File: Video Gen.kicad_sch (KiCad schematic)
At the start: 35 parts, among them J18 Aux Video, K14 VIDEO OUT, Q3 2N3904

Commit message: update traces
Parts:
- removed K14: VIDEO OUT, symbol Connector:Conn_Coaxial_Power
- added K14: RCA Connector, Apple-II:VIDEO, symbol Apple-II:Video
- A10: footprint Package_DIP:DIP-16_W7.62mm_Socket -> Package_DIP:DIP-16_W7.62mm
- A2, B10, B11, B12, B13, B2, C11, C13, C14: footprint Apple:DIP-14_W7.62mm -> Package_DIP:DIP-14_W7.62mm
- A3, A8, A9, B4, B9: footprint Apple:DIP-16_W7.62mm -> Package_DIP:DIP-16_W7.62mm
- A5: footprint Apple:DIP-24_W15.24mm -> Package_DIP:DIP-24_W15.24mm
- B3: footprint Apple:DIP-8_W7.62mm -> Package_DIP:DIP-8_W7.62mm
- Cap13, Cap14: footprint (none) -> Capacitor_THT:C_Disc_D5.0mm_W2.5mm_P5.00mm
- Cap15: renamed from C15; footprint (none) -> Capacitor_THT:C_Disc_D5.0mm_W2.5mm_P5.00mm
- Cap2: footprint (none) -> Capacitor_THT:C_Disc_D7.0mm_W2.5mm_P5.00mm
- L1: footprint (none) -> Inductor_THT:L_Axial_L7.0mm_D3.3mm_P12.70mm_Horizontal_Fastron_MICC
- R10, R12, R13, R5, R9: footprint (none) -> Resistor_THT:R_Axial_DIN0207_L6.3mm_D2.5mm_P10.16mm_Horizontal
- R11: footprint (none) -> Potentiometer_THT:Potentiometer_Bourns_3266Y_Vertical
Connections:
- net GND: now also K14.1
- net at R10.2: now also K14.2
- no-connect marks 6 -> 7
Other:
- moved on the sheet: R10

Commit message: more tracing
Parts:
- K14: DigiKey (none) -> PJRAN1X1U03X-ND
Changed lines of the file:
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@@
       (effects (font (size 1.27 1.27)) hide)
     )
-    (pin "8")
-    (pin "9")
     (pin "1")
     (pin "10")
@@
     (pin "6")
     (pin "7")
+    (pin "8")
+    (pin "9")
     (instances
       (project "AppleII"
@@
     (pin "1")
     (pin "2")
-    (pin "4")
-    (pin "7")
-    (pin "8")
-    (pin "3")
-    (pin "6")
+    (pin "3")
+    (pin "4")
+    (pin "6")
+    (pin "7")
+    (pin "8")
     (instances
       (project "AppleII"
@@
       (effects (font (size 1.27 1.27)) hide)
     )
+    (pin "1")
+    (pin "2")
+    (pin "3")
+    (pin "4")
+    (pin "5")
+    (pin "6")
     (pin "8")
     (pin "9")
+    (pin "10")
     (pin "11")
-    (pin "7")
-    (pin "6")
-    (pin "10")
+    (pin "12")
+    (pin "13")
     (pin "14")
-    (pin "13")
-    (pin "1")
-    (pin "4")
-    (pin "5")
-    (pin "2")
-    (pin "3")
-    (pin "12")
+    (pin "7")
     (instances
       (project "AppleII"
@@
       (effects (font (size 1.27 1.27)) hide)
     )
-    (property "Datasheet" "" (at 215.392 67.31 0)
-      (effects (font (size 1.27 1.27)) hide)
-    )
+    (property "Datasheet" "https://www.switchcraft.com/assets/1/24/pjran1x1u__x_series_cd.pdf?4664" (at 215.392 67.31 0)
+      (effects (font (size 1.27 1.27)) hide)
+    )
+    (property "DigiKey" "PJRAN1X1U03X-ND" (at 215.392 67.31 0)
+      (effects (font (size 1.27 1.27)) hide)
+    )

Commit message: more tracing
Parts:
- removed CT3: 5-50pf, symbol AppleII-rescue:CTRIM_Small-Device
- added CT3: 5-50pF, Apple-II:COLOUR_TRIM, symbol Device:C_Trim_Differential
- J18: footprint (none) -> Connector_PinHeader_2.54mm:PinHeader_1x04_P2.54mm_Vertical
- Q3: footprint digikey-footprints:TO-92-3 -> Package_TO_SOT_THT:TO-92
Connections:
- net GND: now also CT3.1
- net at Cap2.1, L1.1, R5.2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: now also CT3.2
- no-connect marks 7 -> 8
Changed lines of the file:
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@@
   (no_connect (at 425.45 309.88))
   (no_connect (at 425.45 304.8))
+  (no_connect (at 119.38 201.93))
   (no_connect (at 425.45 240.03))
   (no_connect (at 485.14 170.18))
@@
     (stroke (width 0) (type default))
   )
-  (wire (pts (xy 121.92 200.66) (xy 121.92 203.2))
+  (wire (pts (xy 124.46 201.93) (xy 124.46 203.2))
     (stroke (width 0) (type default))
   )
@@
     (stroke (width 0) (type default))
   )
+  (wire (pts (xy 124.46 203.2) (xy 121.92 203.2))
+    (stroke (width 0) (type default))
+  )
   (wire (pts (xy 196.85 71.12) (xy 205.74 71.12))
     (stroke (width 0) (type default))
@@
     (stroke (width 0) (type default))
   )
-  (wire (pts (xy 121.92 195.58) (xy 121.92 191.77))
+  (wire (pts (xy 121.92 194.31) (xy 121.92 191.77))
     (stroke (width 0) (type default))
   )
@@
     )
   )
-  (symbol (lib_id "AppleII-rescue:CTRIM_Small-Device") (at 121.92 198.12 0) (unit 1)
-    (in_bom yes) (on_board yes) (dnp no)
-    (property "Reference" "CT3" (at 117.602 196.596 0)
-      (effects (font (size 1.27 1.27)) (justify left))
-    )
-    (property "Value" "5-50pf" (at 124.46 202.438 90)
-      (effects (font (size 1.27 1.27)) (justify left))
-    )
-    (property "Footprint" "" (at 121.92 198.12 0)
-      (effects (font (size 1.27 1.27)) hide)
-    )
-    (property "Datasheet" "~" (at 121.92 198.12 0)
-      (effects (font (size 1.27 1.27)) hide)
-    )
-    (pin "1")
-    (pin "2")
-    (instances
-      (project "AppleII"
-        (path "/f1f08369-4db3-46f7-9b89-a5d3cfbed55a/00000000-0000-0000-0000-0000632bf564"
-          (reference "CT3") (unit 1)
-        )
-      )
-    )
-  )
   (symbol (lib_id "power:GND") (at 121.92 204.47 0) (unit 1)
     (in_bom yes) (on_board yes) (dnp no)
@@
       (effects (font (size 1.27 1.27)) (justify right))
     )
-    (property "Footprint" "" (at 172.72 59.69 0)
+    (property "Footprint" "Connector_PinHeader_2.54mm:PinHeader_1x04_P2.54mm_Vertical" (at 172.72 59.69 0)
       (effects (font (size 1.27 1.27)) hide)
     )
@@
       (effects (font (size 1.524 1.524)) (justify left))
     )
-    (property "Footprint" "digikey-footprints:TO-92-3" (at 168.91 92.71 0)
+    (property "Footprint" "Package_TO_SOT_THT:TO-92" (at 168.91 92.71 0)
       (effects (font (size 1.524 1.524)) (justify left) hide)
     )
@@
         )
       )
+    )
+  )
+  (symbol (lib_id "Device:C_Trim_Differential") (at 121.92 198.12 180) (unit 1)
+    (in_bom yes) (on_board yes) (dnp no) (fields_autoplaced)
+    (property "Reference" "CT3" (at 127 196.977 0)
+      (effects (font (size 1.27 1.27)) (justify right))
+    )
+    (property "Value" "5-50pF" (at 127 199.517 0)
+      (effects (font (size 1.27 1.27)) (justify right))
+    )
+    (property "Footprint" "Apple-II:COLOUR_TRIM" (at 121.92 198.12 0)
+      (effects (font (size 1.27 1.27)) hide)
+    )
+    (property "Datasheet" "https://www.vishay.com/docs/28528/bfc2808-10mm.pdf" (at 121.92 198.12 0)
+      (effects (font (size 1.27 1.27)) hide)
+    )
+    (property "DigiKey" "BFC280831659-ND" (at 121.92 198.12 0)
+      (effects (font (size 1.27 1.27)) hide)
+    )
+    (pin "1")
+    (pin "2")
+    (pin "3")
+    (instances
+      (project "AppleII"
+        (path "/f1f08369-4db3-46f7-9b89-a5d3cfbed55a/00000000-0000-0000-0000-0000632bf564"
+          (reference "CT3") (unit 1)
+        )
+      )

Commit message: more tracing
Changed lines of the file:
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@@
-    (stroke (width 0) (type default))
-  )
-  (bus_entry (at 302.26 135.89) (size 2.54 2.54)
     (stroke (width 0) (type default))
   )
@@
     (stroke (width 0) (type default))
   )
-  (bus_entry (at 302.26 138.43) (size 2.54 2.54)
-    (stroke (width 0) (type default))
-  )
   (bus_entry (at 395.224 242.57) (size 2.54 2.54)
     (stroke (width 0) (type default))
   )
-  (bus_entry (at 302.26 133.35) (size 2.54 2.54)
-    (stroke (width 0) (type default))
-  )
   (bus_entry (at 395.224 234.95) (size 2.54 2.54)
     (stroke (width 0) (type default))
@@
     (stroke (width 0) (type default))
   )
-  (bus (pts (xy 294.64 130.81) (xy 302.26 130.81))
-    (stroke (width 0) (type default))
-  )
   (wire (pts (xy 36.83 374.65) (xy 34.29 374.65))
     (stroke (width 0) (type default))
@@
     (stroke (width 0) (type default))
   )
-  (bus (pts (xy 302.26 133.35) (xy 302.26 130.81))
-    (stroke (width 0) (type default))
-  )
   (wire (pts (xy 153.67 95.25) (xy 157.48 95.25))
     (stroke (width 0) (type default))
@@
     (stroke (width 0) (type default))
   )
-  (bus (pts (xy 302.26 138.43) (xy 302.26 135.89))
-    (stroke (width 0) (type default))
-  )
   (wire (pts (xy 149.86 63.5) (xy 149.86 64.77))
     (stroke (width 0) (type default))
@@
   )
   (wire (pts (xy 304.8 146.05) (xy 311.15 146.05))
-    (stroke (width 0) (type default))
-  )
-  (bus (pts (xy 302.26 135.89) (xy 302.26 133.35))
     (stroke (width 0) (type default))
   )
@@
     )
   )
+  (global_label "VB" (shape input) (at 304.8227 138.43 180) (fields_autoplaced)
+    (effects (font (size 1.27 1.27)) (justify right))
+    (property "Intersheetrefs" "${INTERSHEET_REFS}" (at 300.1331 138.43 0)
+      (effects (font (size 1.27 1.27)) (justify right) hide)
+    )
+  )
   (global_label "HIRES" (shape output) (at 151.13 325.12 0)
     (effects (font (size 1.27 1.27)) (justify left))
@@
     )
   )
+  (global_label "VA" (shape input) (at 304.8227 135.89 180) (fields_autoplaced)
+    (effects (font (size 1.27 1.27)) (justify right))
+    (property "Intersheetrefs" "${INTERSHEET_REFS}" (at 300.3145 135.89 0)
+      (effects (font (size 1.27 1.27)) (justify right) hide)
+    )
+  )
   (global_label "V2" (shape input) (at 43.942 322.58 180)
     (effects (font (size 1.27 1.27)) (justify right))
@@
     )
   )
-  (global_label "V[A..C]" (shape input) (at 294.64 130.81 180)
-    (effects (font (size 1.27 1.27)) (justify right))
-    (property "Intersheetrefs" "${INTERSHEET_REFS}" (at 294.64 130.81 0)
-      (effects (font (size 1.27 1.27)) hide)
-    )
-  )
   (global_label "LD[0..7]" (shape input) (at 395.224 232.918 0)
     (effects (font (size 1.27 1.27)) (justify left))
@@
     )
   )
+  (global_label "VC" (shape input) (at 304.8227 140.97 180) (fields_autoplaced)
+    (effects (font (size 1.27 1.27)) (justify right))
+    (property "Intersheetrefs" "${INTERSHEET_REFS}" (at 300.1331 140.97 0)
+      (effects (font (size 1.27 1.27)) (justify right) hide)
+    )
+  )

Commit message: finish tracing
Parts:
- added unit 7 of C11
- added unit 3 of C13
- added Cap16: 0.1uF, Capacitor_THT:C_Disc_D5.0mm_W2.5mm_P5.00mm, symbol Device:C_Small
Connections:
- net A8-6 is gone; now on net GND: A8.6 (I1b)
- net +5V: now also C11.14 (VCC), C13.14 (VCC), Cap16.2
- net GND: now also C11.7 (GND), C13.7 (GND), Cap16.1
- net A9-9 renamed B11-5

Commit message: beautify capacitor footprint
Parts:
- renumbered Cap16 to Cap47
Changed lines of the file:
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@@
   (symbol (lib_id "Device:C_Small") (at 499.11 182.88 270) (unit 1)
     (in_bom yes) (on_board yes) (dnp no)
-    (property "Reference" "Cap16" (at 500.888 183.134 0)
+    (property "Reference" "Cap47" (at 500.888 183.134 0)
       (effects (font (size 1.27 1.27)) (justify left))
     )
@@
     (instances
       (project "AppleII"
-        (path "/f1f08369-4db3-46f7-9b89-a5d3cfbed55a/00000000-0000-0000-0000-00006017a131"
-          (reference "Cap16") (unit 1)
-        )
         (path "/f1f08369-4db3-46f7-9b89-a5d3cfbed55a/00000000-0000-0000-0000-0000632bf564"
           (reference "Cap47") (unit 1)
@@
   (symbol (lib_id "power:GND") (at 501.65 182.88 90) (unit 1)
     (in_bom yes) (on_board yes) (dnp no)
-    (property "Reference" "#PWR015" (at 508 182.88 0)
+    (property "Reference" "#PWR03" (at 508 182.88 0)
       (effects (font (size 1.27 1.27)) hide)
     )
@@
     (instances
       (project "AppleII"
-        (path "/f1f08369-4db3-46f7-9b89-a5d3cfbed55a/00000000-0000-0000-0000-00006017a131"
-          (reference "#PWR015") (unit 1)
-        )
         (path "/f1f08369-4db3-46f7-9b89-a5d3cfbed55a/00000000-0000-0000-0000-0000632bf564"
           (reference "#PWR03") (unit 1)

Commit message: beautify resistors
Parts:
- Cap13, Cap14, Cap15, Cap47: footprint Capacitor_THT:C_Disc_D5.0mm_W2.5mm_P5.00mm -> Apple-II:C_Disc_D5.0mm_W2.5mm_P5.00mm
- R10, R12, R13, R5, R6, R7, R8, R9: footprint Resistor_THT:R_Axial_DIN0207_L6.3mm_D2.5mm_P10.16mm_Horizontal -> Apple-II:R_Axial_DIN0207_L6.3mm_D2.5mm_P10.16mm_Horizontal
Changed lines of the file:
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@@
       (effects (font (size 1.27 1.27)))
     )
-    (property "Footprint" "Resistor_THT:R_Axial_DIN0207_L6.3mm_D2.5mm_P10.16mm_Horizontal" (at 96.52 193.548 90)
+    (property "Footprint" "Apple-II:R_Axial_DIN0207_L6.3mm_D2.5mm_P10.16mm_Horizontal" (at 96.52 193.548 90)
       (effects (font (size 1.27 1.27)) hide)
     )
@@
       (effects (font (size 1.27 1.27)))
     )
-    (property "Footprint" "Resistor_THT:R_Axial_DIN0207_L6.3mm_D2.5mm_P10.16mm_Horizontal" (at 199.136 65.278 90)
+    (property "Footprint" "Apple-II:R_Axial_DIN0207_L6.3mm_D2.5mm_P10.16mm_Horizontal" (at 199.136 65.278 90)
       (effects (font (size 1.27 1.27)) hide)
     )
@@
       (effects (font (size 1.27 1.27)) (justify left))
     )
-    (property "Footprint" "Capacitor_THT:C_Disc_D5.0mm_W2.5mm_P5.00mm" (at 160.02 62.23 0)
+    (property "Footprint" "Apple-II:C_Disc_D5.0mm_W2.5mm_P5.00mm" (at 160.02 62.23 0)
       (effects (font (size 1.27 1.27)) hide)
     )
@@
       (effects (font (size 1.27 1.27)) (justify left))
     )
-    (property "Footprint" "Capacitor_THT:C_Disc_D5.0mm_W2.5mm_P5.00mm" (at 149.86 60.96 0)
+    (property "Footprint" "Apple-II:C_Disc_D5.0mm_W2.5mm_P5.00mm" (at 149.86 60.96 0)
       (effects (font (size 1.27 1.27)) hide)
     )
@@
       (effects (font (size 1.27 1.27)))
     )
-    (property "Footprint" "Resistor_THT:R_Axial_DIN0207_L6.3mm_D2.5mm_P10.16mm_Horizontal" (at 317.246 68.072 90)
+    (property "Footprint" "Apple-II:R_Axial_DIN0207_L6.3mm_D2.5mm_P10.16mm_Horizontal" (at 317.246 68.072 90)
       (effects (font (size 1.27 1.27)) hide)
     )
@@
       (effects (font (size 1.27 1.27)) (justify left))
     )
-    (property "Footprint" "Capacitor_THT:C_Disc_D5.0mm_W2.5mm_P5.00mm" (at 315.468 76.962 0)
+    (property "Footprint" "Apple-II:C_Disc_D5.0mm_W2.5mm_P5.00mm" (at 315.468 76.962 0)
       (effects (font (size 1.27 1.27)) hide)
     )
@@
       (effects (font (size 1.27 1.27)))
     )
-    (property "Footprint" "Resistor_THT:R_Axial_DIN0207_L6.3mm_D2.5mm_P10.16mm_Horizontal" (at 317.246 60.452 90)
+    (property "Footprint" "Apple-II:R_Axial_DIN0207_L6.3mm_D2.5mm_P10.16mm_Horizontal" (at 317.246 60.452 90)
       (effects (font (size 1.27 1.27)) hide)
     )
@@
       (effects (font (size 1.27 1.27)))
     )
-    (property "Footprint" "Resistor_THT:R_Axial_DIN0207_L6.3mm_D2.5mm_P10.16mm_Horizontal" (at 165.1 127.762 90)
+    (property "Footprint" "Apple-II:R_Axial_DIN0207_L6.3mm_D2.5mm_P10.16mm_Horizontal" (at 165.1 127.762 90)
       (effects (font (size 1.27 1.27)) hide)
     )
@@
       (effects (font (size 1.27 1.27)))
     )
-    (property "Footprint" "Resistor_THT:R_Axial_DIN0207_L6.3mm_D2.5mm_P10.16mm_Horizontal" (at 175.768 143.51 90)
+    (property "Footprint" "Apple-II:R_Axial_DIN0207_L6.3mm_D2.5mm_P10.16mm_Horizontal" (at 175.768 143.51 90)
       (effects (font (size 1.27 1.27)) hide)
     )
@@
       (effects (font (size 1.27 1.27)))
     )
-    (property "Footprint" "Resistor_THT:R_Axial_DIN0207_L6.3mm_D2.5mm_P10.16mm_Horizontal" (at 184.15 131.318 90)
+    (property "Footprint" "Apple-II:R_Axial_DIN0207_L6.3mm_D2.5mm_P10.16mm_Horizontal" (at 184.15 131.318 90)
       (effects (font (size 1.27 1.27)) hide)
     )
@@
       (effects (font (size 1.27 1.27)))
     )
-    (property "Footprint" "Resistor_THT:R_Axial_DIN0207_L6.3mm_D2.5mm_P10.16mm_Horizontal" (at 161.29 97.028 90)
+    (property "Footprint" "Apple-II:R_Axial_DIN0207_L6.3mm_D2.5mm_P10.16mm_Horizontal" (at 161.29 97.028 90)
       (effects (font (size 1.27 1.27)) hide)
     )
@@
       (effects (font (size 1.27 1.27)) (justify left))
     )
-    (property "Footprint" "Capacitor_THT:C_Disc_D5.0mm_W2.5mm_P5.00mm" (at 499.11 182.88 0)
-      (effects (font (size 1.27 1.27)) hide)
-    )
+    (property "Footprint" "Apple-II:C_Disc_D5.0mm_W2.5mm_P5.00mm" (at 499.11 182.88 0)
+      (effects (font (size 1.27 1.27)) hide)
+    )

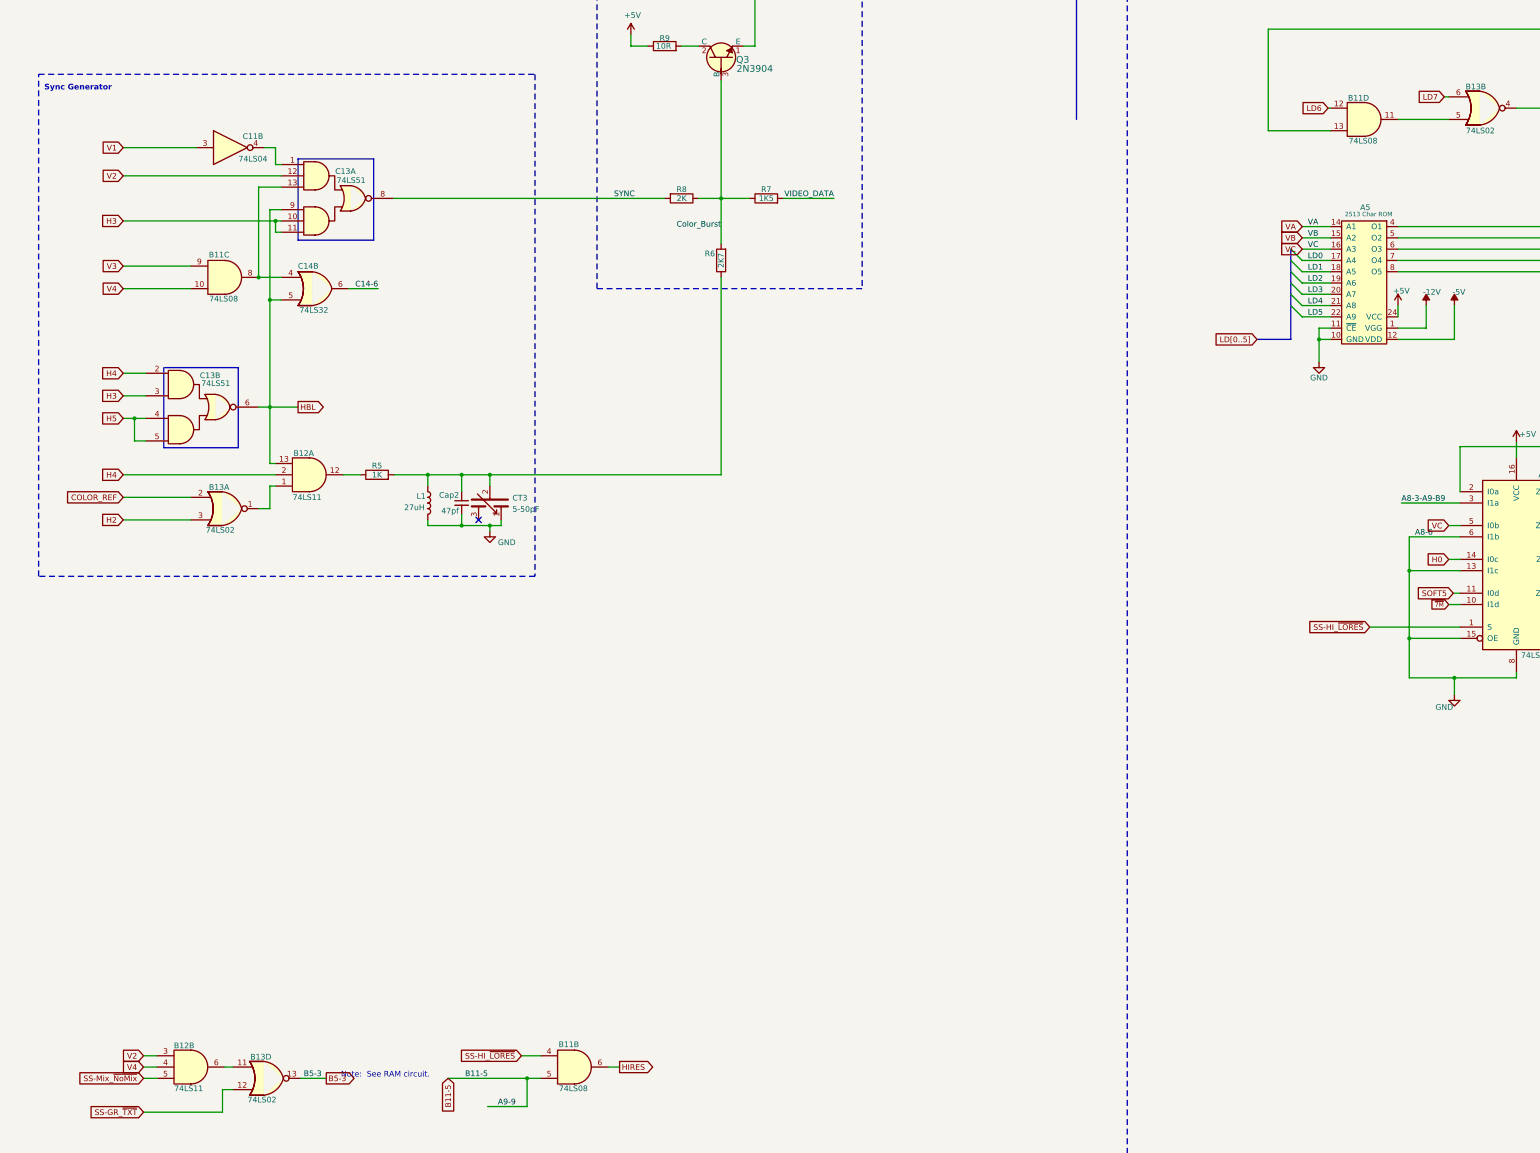
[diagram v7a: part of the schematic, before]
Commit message: add missing test points
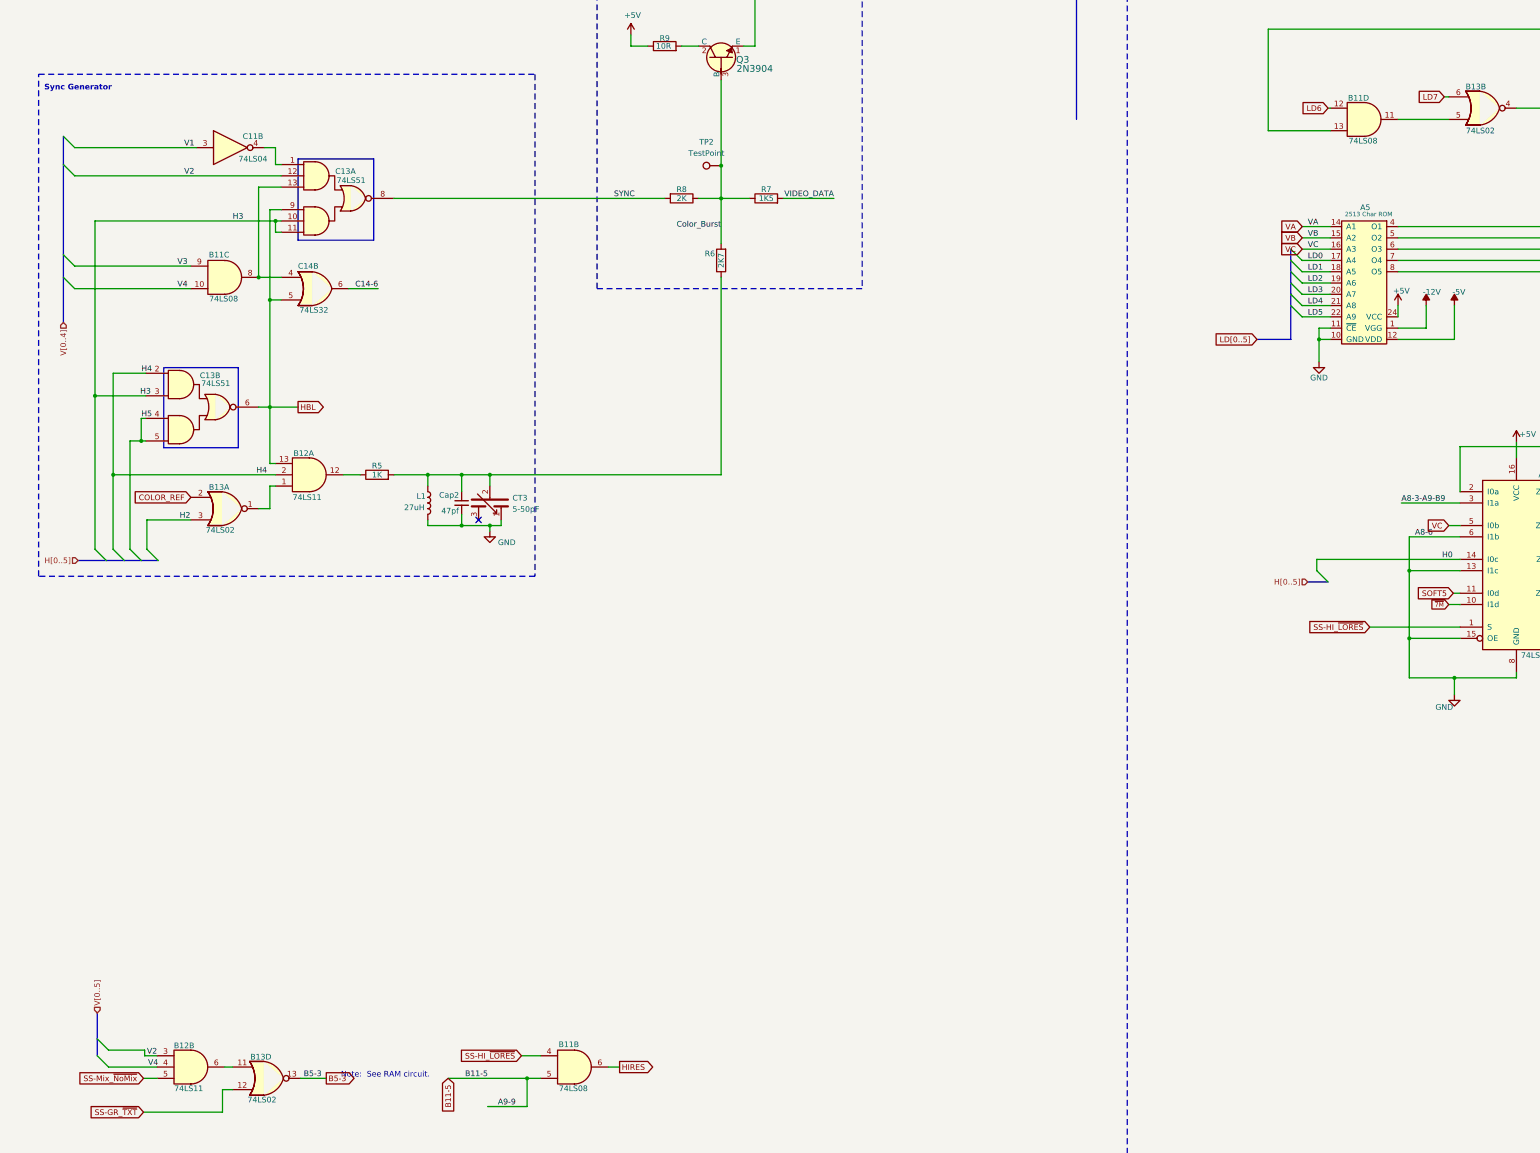
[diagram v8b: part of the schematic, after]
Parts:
- added TP2: TestPoint, TestPoint:TestPoint_THTPad_1.5x1.5mm_Drill0.7mm, symbol Connector:TestPoint
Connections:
- net Color_Burst: now also TP2.1
